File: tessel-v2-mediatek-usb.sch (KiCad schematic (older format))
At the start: 38 parts, among them J901 USB_A_2_stack, U201 MT7620N, U901 AIC1528-0PSTR, U902 FE1.1, X901 12MHz

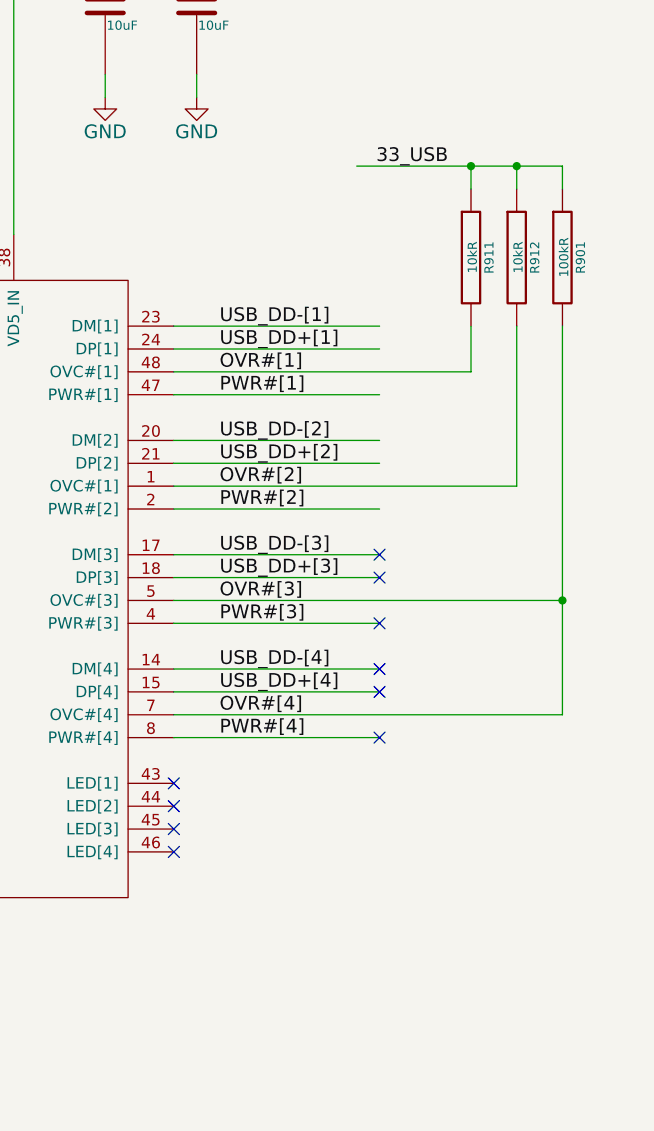
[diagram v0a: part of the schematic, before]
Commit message: added nasty RC time constant hack to USB overcurrent flags
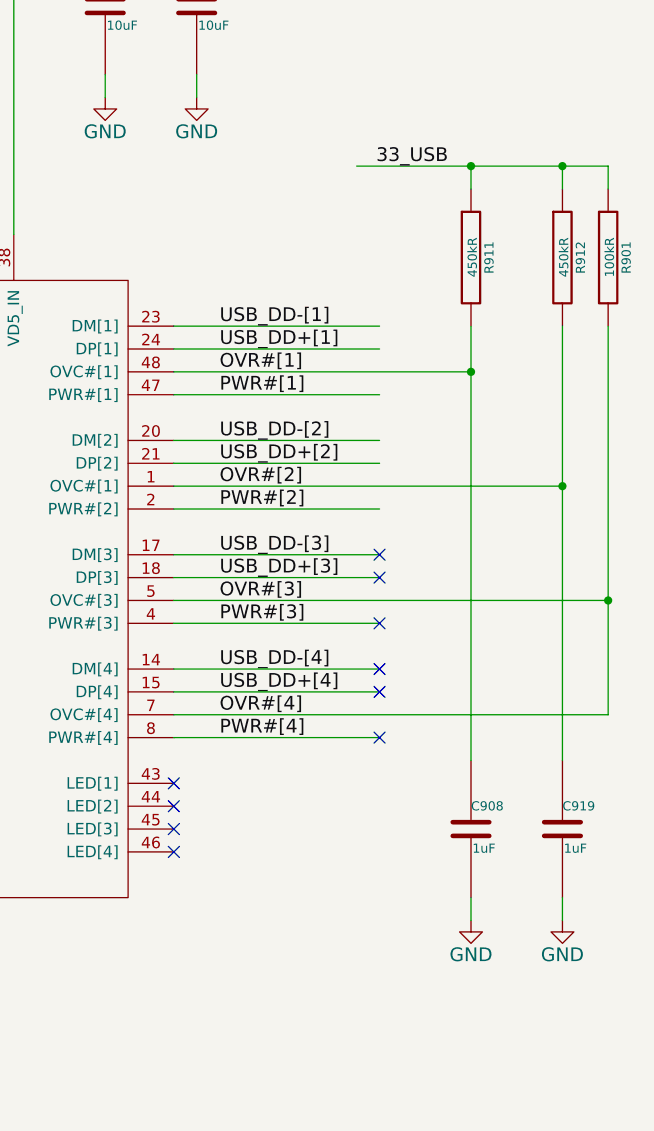
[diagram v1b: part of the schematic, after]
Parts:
- added C908, C919: 1uF, tm-kicad-lib:SMD-0402-C, symbol TM_C
- R911, R912: value 10kR -> 450kR
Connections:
- wire segments 165 -> 167
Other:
- moved on the sheet: R901, R912
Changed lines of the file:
@@
 	14200 5800 15100 5800
 Wire Wire Line
-	14200 5900 15700 5900
+	14200 5900 15900 5900
 Wire Wire Line
 	14200 6000 15100 6000
@@
 	14200 6300 15100 6300
 Wire Wire Line
-	14200 6400 15900 6400
+	14200 6400 16100 6400
 Wire Wire Line
 	14200 6500 15100 6500
@@
 L TM_R R901
 U 1 1 550733F2
-P 15900 4900
-F 0 "R901" V 15980 4900 40  0000 C CNN
-F 1 "100kR" V 15907 4901 40  0000 C CNN
-F 2 "tm-kicad-lib:SMD-0402-R" V 15830 4900 30  0001 C CNN
-F 3 "" H 15900 4900 30  0000 C CNN
-	1    15900 4900
+P 16100 4900
+F 0 "R901" V 16180 4900 40  0000 C CNN
+F 1 "100kR" V 16107 4901 40  0000 C CNN
+F 2 "tm-kicad-lib:SMD-0402-R" V 16030 4900 30  0001 C CNN
+F 3 "" H 16100 4900 30  0000 C CNN
+	1    16100 4900
 	1    0    0    -1
 $EndComp
@@
 33_USB
 Wire Wire Line
-	15000 4500 15900 4500
-Wire Wire Line
-	15900 4500 15900 4600
-Connection ~ 15900 6400
+	15000 4500 16100 4500
+Wire Wire Line
+	16100 4500 16100 4600
+Connection ~ 16100 6400
 $Comp
 L TM_R R911
@@
 P 15500 4900
 F 0 "R911" V 15580 4900 40  0000 C CNN
-F 1 "10kR" V 15507 4901 40  0000 C CNN
+F 1 "450kR" V 15507 4901 40  0000 C CNN
 F 2 "tm-kicad-lib:SMD-0402-R" V 15430 4900 30  0001 C CNN
 F 3 "" H 15500 4900 30  0000 C CNN
@@
 L TM_R R912
 U 1 1 550C6C1C
-P 15700 4900
-F 0 "R912" V 15780 4900 40  0000 C CNN
-F 1 "10kR" V 15707 4901 40  0000 C CNN
-F 2 "tm-kicad-lib:SMD-0402-R" V 15630 4900 30  0001 C CNN
-F 3 "" H 15700 4900 30  0000 C CNN
-	1    15700 4900
+P 15900 4900
+F 0 "R912" V 15980 4900 40  0000 C CNN
+F 1 "450kR" V 15907 4901 40  0000 C CNN
+F 2 "tm-kicad-lib:SMD-0402-R" V 15830 4900 30  0001 C CNN
+F 3 "" H 15900 4900 30  0000 C CNN
+	1    15900 4900
 	1    0    0    -1
 $EndComp
@@
 Connection ~ 15500 4500
 Wire Wire Line
-	15700 4600 15700 4500
-Connection ~ 15700 4500
-Wire Wire Line
-	15500 5400 15500 5200
-Wire Wire Line
-	15700 5900 15700 5200
+	15900 4600 15900 4500
+Connection ~ 15900 4500
+Wire Wire Line
+	15500 5200 15500 7100
+Wire Wire Line
+	15900 5200 15900 7100
 $Comp
 L TM_R R902
@@
 POWER\nSWITCH\nBYPASS
 Wire Wire Line
-	15900 6900 14200 6900
-Wire Wire Line
-	15900 5200 15900 6900
+	16100 6900 14200 6900
+Wire Wire Line
+	16100 5200 16100 6900
+$Comp
+L TM_C C919
+U 1 1 55306223
+P 15900 7400
+F 0 "C919" H 15900 7500 40  0000 L CNN
+F 1 "1uF" H 15906 7315 40  0000 L CNN
+F 2 "tm-kicad-lib:SMD-0402-C" H 15938 7250 30  0001 C CNN
+F 3 "" H 15900 7400 60  0000 C CNN
+	1    15900 7400
+	1    0    0    -1
+$EndComp
+$Comp
+L GND #PWR0222
+U 1 1 55306229
+P 15900 7800
+F 0 "#PWR0222" H 15900 7550 60  0001 C CNN
+F 1 "GND" H 15900 7650 60  0000 C CNN
+F 2 "" H 15900 7800 60  0000 C CNN
+F 3 "" H 15900 7800 60  0000 C CNN
+	1    15900 7800
+	1    0    0    -1
+$EndComp
+Wire Wire Line
+	15900 7800 15900 7700
+$Comp
+L TM_C C908
+U 1 1 5530626A
+P 15500 7400
+F 0 "C908" H 15500 7500 40  0000 L CNN
+F 1 "1uF" H 15506 7315 40  0000 L CNN
+F 2 "tm-kicad-lib:SMD-0402-C" H 15538 7250 30  0001 C CNN
+F 3 "" H 15500 7400 60  0000 C CNN
+	1    15500 7400
+	1    0    0    -1
+$EndComp
+$Comp
+L GND #PWR0223
+U 1 1 55306270
+P 15500 7800
+F 0 "#PWR0223" H 15500 7550 60  0001 C CNN
+F 1 "GND" H 15500 7650 60  0000 C CNN
+F 2 "" H 15500 7800 60  0000 C CNN
+F 3 "" H 15500 7800 60  0000 C CNN
+	1    15500 7800
+	1    0    0    -1
+$EndComp
+Wire Wire Line
+	15500 7800 15500 7700
+Connection ~ 15500 5400
+Connection ~ 15900 5900
 $EndSCHEMATC

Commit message: schematic cleanup
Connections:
- wire segments 167 -> 214
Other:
- moved on the sheet: C906, C908, C910, C911, C912, C913, C914, C915, C916, C917, C918, C919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

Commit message: pushed changes through to layout, passes DRC
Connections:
- wire segments 214 -> 167
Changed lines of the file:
@@
 	13700 4200 13700 4100
 Wire Wire Line
-	13300 3400 13700 3400
-Wire Wire Line
-	13700 3400 14100 3400
+	13300 3400 14100 3400
 Wire Wire Line
 	10700 9200 10700 9300
@@
 	2000 2300 1300 2300
 Wire Wire Line
-	5400 2100 6200 2100
-Wire Wire Line
-	6200 2100 6300 2100
+	5400 2100 6300 2100
 Wire Wire Line
 	6200 2100 6200 2200
@@
 	7000 2200 7000 2100
 Wire Wire Line
-	6900 2100 7000 2100
-Wire Wire Line
-	7000 2100 7600 2100
+	6900 2100 7600 2100
 Connection ~ 6200 2100
 Connection ~ 7000 2100
@@
 	7000 2900 7000 2800
 Wire Wire Line
-	5400 900  6200 900
-Wire Wire Line
-	6200 900  6300 900
+	5400 900  6300 900
 Wire Wire Line
 	6200 900  6200 1000
@@
 	7000 1000 7000 900
 Wire Wire Line
-	6900 900  7000 900
-Wire Wire Line
-	7000 900  7600 900
+	6900 900  7600 900
 Connection ~ 6200 900
 Connection ~ 7000 900
@@
 	3500 2300 3400 2300
 Wire Wire Line
-	3400 2100 4400 2100
-Wire Wire Line
-	4400 2100 4600 2100
-Wire Wire Line
-	3400 1900 4200 1900
-Wire Wire Line
-	4200 1900 4600 1900
+	3400 2100 4600 2100
+Wire Wire Line
+	3400 1900 4600 1900
 Wire Wire Line
 	1900 1700 2000 1700
@@
 	14100 3400 14100 3500
 Wire Wire Line
-	13300 3300 13300 3400
-Wire Wire Line
-	13300 3400 13300 4800
+	13300 3300 13300 4800
 Connection ~ 13300 3400
 Wire Wire Line
@@
 	11700 4200 11700 4100
 Wire Wire Line
-	10500 3400 10900 3400
-Wire Wire Line
-	10900 3400 11300 3400
-Wire Wire Line
-	11300 3400 11700 3400
-Wire Wire Line
-	11700 3400 12200 3400
+	10500 3400 12200 3400
 Wire Wire Line
 	11700 3400 11700 3500
@@
 	13300 1900 13300 2000
 Wire Wire Line
-	12800 1900 13300 1900
-Wire Wire Line
-	13300 1900 13700 1900
-Wire Wire Line
-	13700 1900 14100 1900
-Wire Wire Line
-	14100 1900 14500 1900
-Wire Wire Line
-	12400 4600 12500 4600
-Wire Wire Line
-	12500 4600 12600 4600
-Wire Wire Line
-	12600 4600 12700 4600
-Wire Wire Line
-	12700 4600 12800 4600
-Wire Wire Line
-	12800 4600 12900 4600
-Wire Wire Line
-	12900 4600 13100 4600
+	12800 1900 14500 1900
+Wire Wire Line
+	12400 4600 13100 4600
 Wire Wire Line
 	12900 4600 12900 4800
@@
 	9900 5500 9900 5600
 Wire Wire Line
-	9900 5600 10900 5600
-Wire Wire Line
-	10900 5600 11000 5600
+	9900 5600 11000 5600
 Wire Wire Line
 	10900 5400 10900 5600
@@
 	11000 6100 10100 6100
 Wire Wire Line
-	12200 3400 12200 4600
-Wire Wire Line
-	12200 4600 12200 4800
+	12200 3400 12200 4800
 Wire Wire Line
 	11700 4600 11700 4800
 Wire Wire Line
-	11700 4600 11900 4600
-Wire Wire Line
-	11900 4600 12000 4600
-Wire Wire Line
-	12000 4600 12200 4600
+	11700 4600 12200 4600
 Connection ~ 12200 4600
 Wire Wire Line
@@
 	10900 7500 11000 7500
 Wire Wire Line
-	10500 9200 10700 9200
-Wire Wire Line
-	10700 9200 11500 9200
+	10500 9200 11500 9200
 Connection ~ 10700 9200
 Wire Wire Line
@@
 	9700 10000 9700 9900
 Wire Wire Line
-	8800 9200 9700 9200
-Wire Wire Line
-	9700 9200 9900 9200
+	8800 9200 9900 9200
 Wire Wire Line
 	9700 9300 9700 9200
@@
 Connection ~ 6300 3700
 Wire Wire Line
-	5900 3700 6000 3700
-Wire Wire Line
-	6000 3700 6300 3700
-Wire Wire Line
-	6300 3700 6700 3700
+	5900 3700 6700 3700
 Wire Wire Line
 	6700 3700 6700 3800
@@
 	6300 4400 6300 4500
 Wire Wire Line
-	6700 4400 6700 4500
-Wire Wire Line
-	6700 4500 6700 4600
+	6700 4400 6700 4600
 Wire Wire Line
 	4900 4600 4900 4700
@@
 	4900 4700 5000 4700
 Wire Wire Line
-	5000 4600 5000 4700
-Wire Wire Line
-	5000 4700 5000 4800
+	5000 4600 5000 4800
 Connection ~ 5000 4700
 Wire Wire Line
@@
 Connection ~ 6000 3900
 Wire Wire Line
-	6000 3700 6000 3800
-Wire Wire Line
-	6000 3800 6000 3900
-Wire Wire Line
-	6000 3900 6000 4000
+	6000 3700 6000 4000
 Wire Wire Line
 	6300 3700 6300 3800
@@
 	5000 3000 5000 3200
 Wire Wire Line
-	1300 3600 3400 3600
-Wire Wire Line
-	3400 3600 4100 3600
-Wire Wire Line
-	1300 3700 3500 3700
-Wire Wire Line
-	3500 3700 4100 3700
-Wire Wire Line
-	1300 4100 2100 4100
-Wire Wire Line
-	2100 4100 4100 4100
-Wire Wire Line
-	1300 4200 2200 4200
-Wire Wire Line
-	2200 4200 4100 4200
+	1300 3600 4100 3600
+Wire Wire Line
+	1300 3700 4100 3700
+Wire Wire Line
+	1300 4100 4100 4100
+Wire Wire Line
+	1300 4200 4100 4200
 Wire Wire Line
 	2100 4800 2100 4100
@@
 Connection ~ 3500 3700
 Wire Wire Line
-	12100 7900 12100 8000
-Wire Wire Line
-	12100 8000 12100 8100
-Wire Wire Line
-	12100 8000 12300 8000
-Wire Wire Line
-	12300 8000 12400 8000
-Wire Wire Line
-	12400 8000 12500 8000
-Wire Wire Line
-	12500 8000 12600 8000
-Wire Wire Line
-	12600 8000 12800 8000
+	12100 7900 12100 8100
+Wire Wire Line
+	12100 8000 12800 8000
 Wire Wire Line
 	12800 8000 12800 7900
@@
 $EndComp
 Wire Wire Line
-	14500 1600 14500 1900
-Wire Wire Line
-	14500 1900 14500 2000
+	14500 1600 14500 2000
 Text Label 9500 4800 0    60   ~ 0
 33_USB
@@
 33_USB
 Wire Wire Line
-	14800 4500 15300 4500
-Wire Wire Line
-	15300 4500 15700 4500
-Wire Wire Line
-	15700 4500 16100 4500
+	14800 4500 16100 4500
 Wire Wire Line
 	16100 4500 16100 4600
@@
 Connection ~ 15700 4500
 Wire Wire Line
-	15300 5200 15300 5400
-Wire Wire Line
-	15300 5400 15300 7100
-Wire Wire Line
-	15700 5200 15700 5900
-Wire Wire Line
-	15700 5900 15700 7100
+	15300 5200 15300 7100
+Wire Wire Line
+	15700 5200 15700 7100
 $Comp
 L TM_R R902
@@
 $EndComp
 Wire Wire Line
-	4200 1000 4200 1100
-Wire Wire Line
-	4200 1100 4200 1200
+	4200 1000 4200 1200
 Wire Wire Line
 	4200 1100 4400 1100
@@
 	16100 6900 14000 6900
 Wire Wire Line
-	16100 5200 16100 6400
-Wire Wire Line
-	16100 6400 16100 6900
+	16100 5200 16100 6900
 $Comp
 L TM_C C919

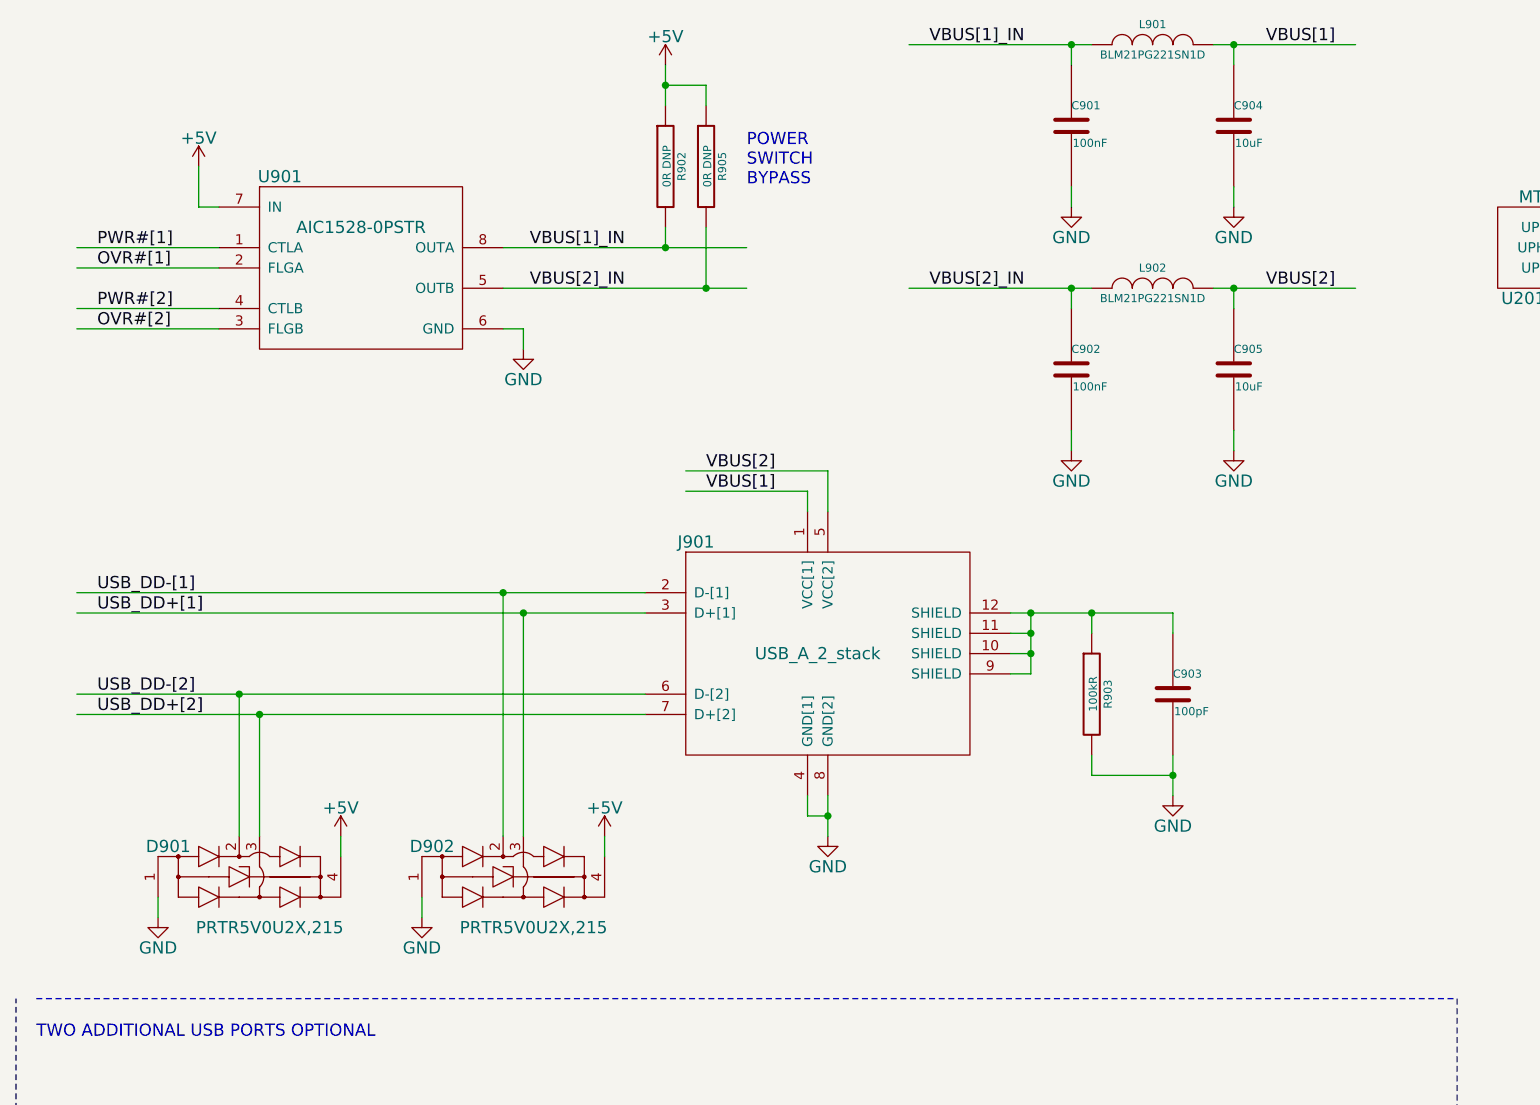
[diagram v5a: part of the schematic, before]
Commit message: addresses EMC issues, adds placeholder FCC, CE, etc. silk
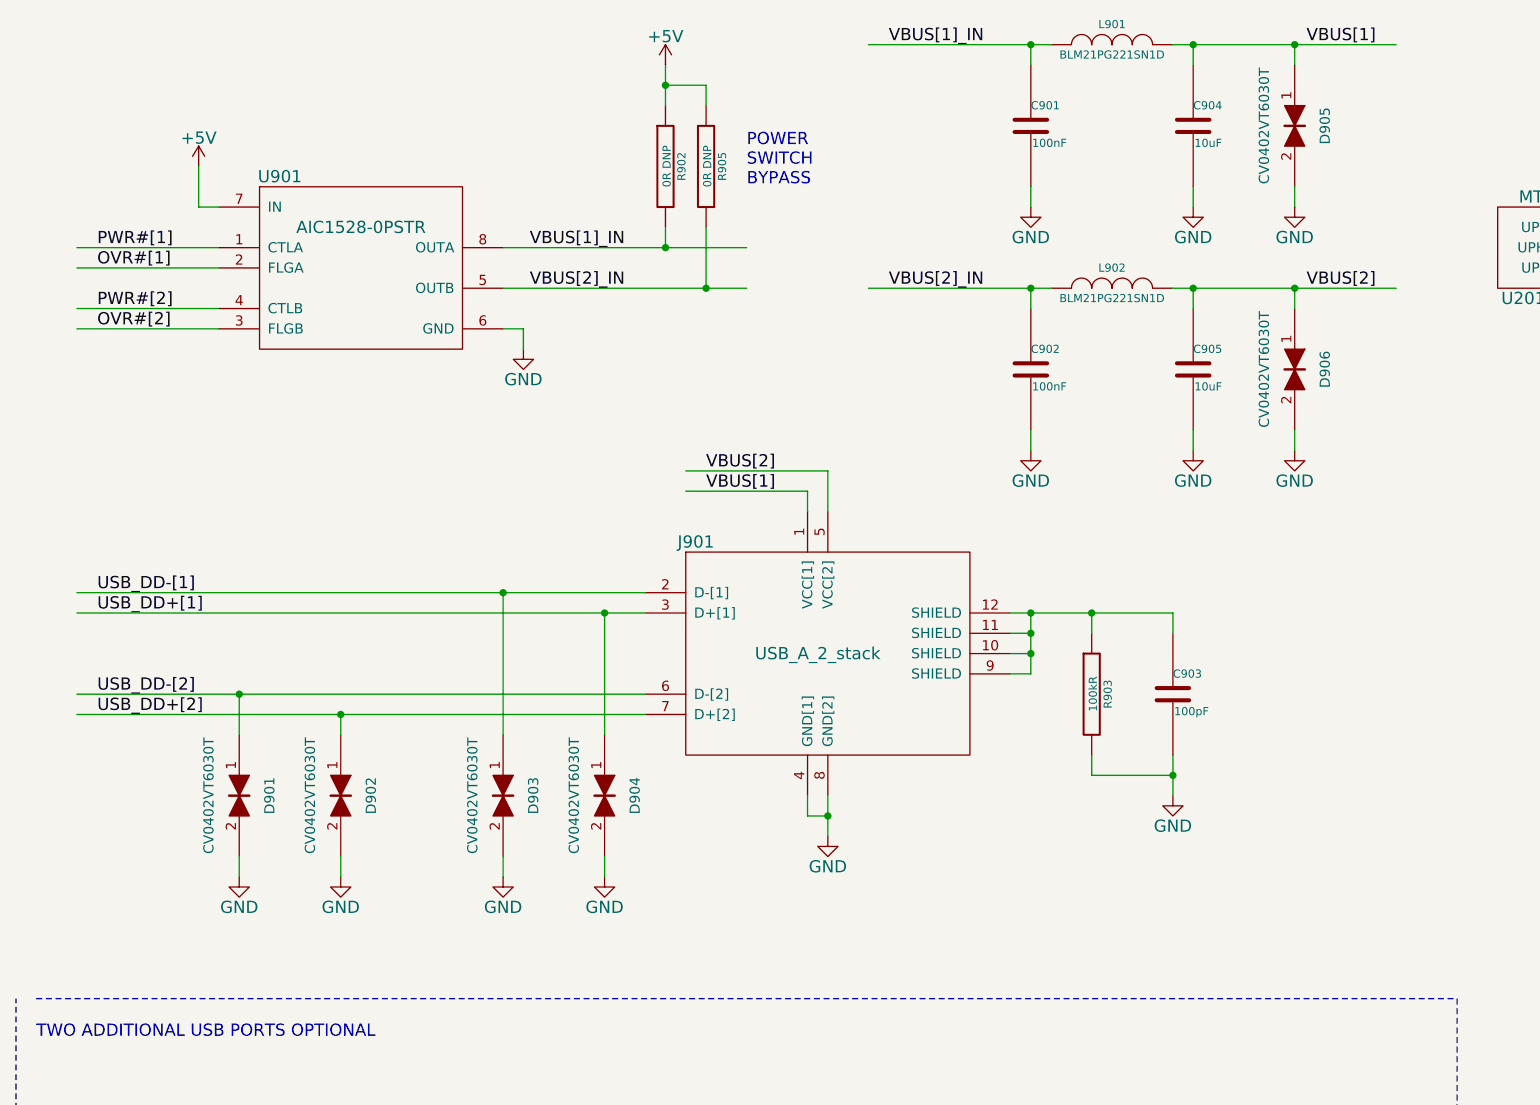
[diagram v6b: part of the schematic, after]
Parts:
- removed D901, D902: PRTR5V0U2X,215, tm-kicad-lib:PRTR5V0U2X,215, symbol PRTR5V0U2X,215
- added D901, D902, D903, D904, D905, D906: CV0402VT6030T, tm-kicad-lib:SMD-0402-R, symbol TVS
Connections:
- wire segments 167 -> 171
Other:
- moved on the sheet: C901, C902, C904, C905, L901, L902
